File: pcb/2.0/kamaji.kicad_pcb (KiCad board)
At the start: 2 copper layers, 100 x 100 mm, 92 parts, among them J1 RJ10, J2 RJ10, J3 RJ10, J4 RJ10, J5 RJ10, J6 RJ10, J7 USB_B, J8 USB_A, Q1 2N3904, Q2 IRL540N, Q3 IRL540N, SW1 SW_Push, SW2 SW_Push, SW3 SW_Push, U1 ATMEGA32U4-AU, Y1 16MHz

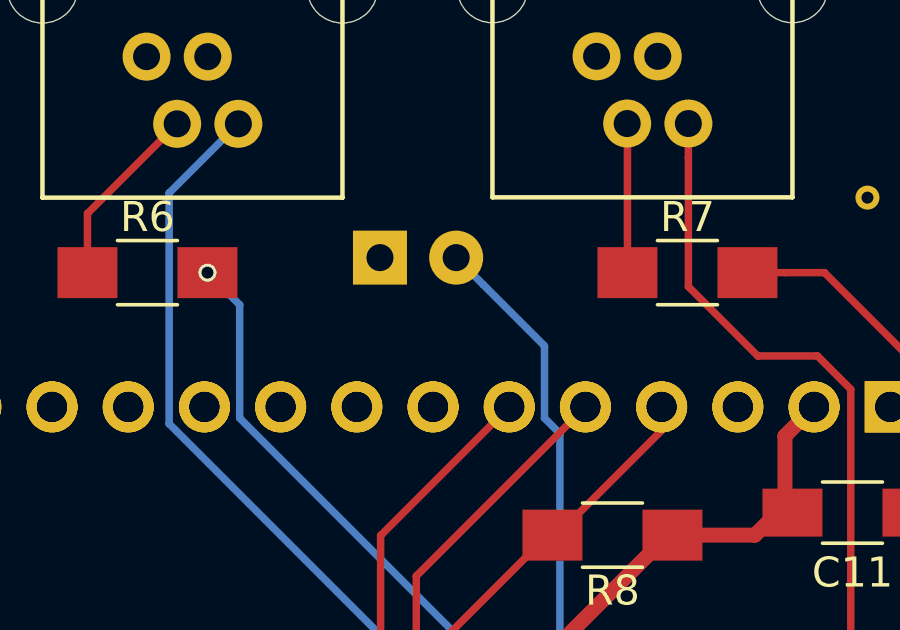
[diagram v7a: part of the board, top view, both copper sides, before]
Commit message: move the LED a bit
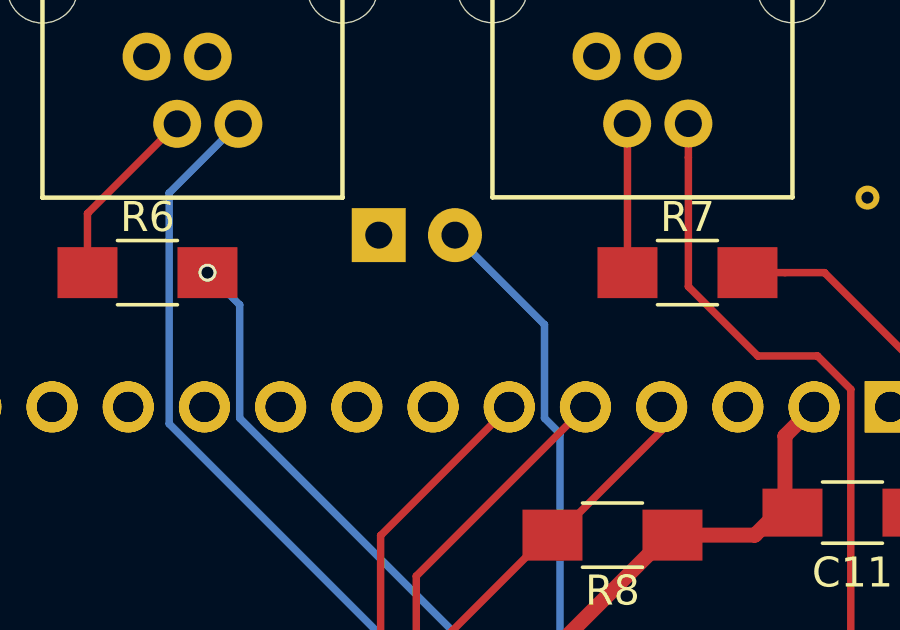
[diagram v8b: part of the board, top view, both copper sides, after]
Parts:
- moved D1 0.75 mm to (98.7, 61.2)
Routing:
- net /SIGNAL_LED: track 33.9 -> 34.7 mm
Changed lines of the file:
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@@
     (links 203)
     (no_connects 1)
-    (area 42.564999 46.54 152.093 150.075001)
+    (area 49.924999 49.924999 150.075001 150.075001)
     (thickness 1.6)
     (drawings 9)
-    (tracks 450)
+    (tracks 449)
     (zones 0)
     (modules 92)
@@
   )
   (module LEDs:LED_D5.0mm (layer B.Cu)
-    (at 98.75 62)
+    (at 98.71 61.25)
     (descr "LED, diameter 5.0mm, 2 pins, http://cdn-reichelt.de/documents/datenblatt/A500/LL-504BC2E-009.pdf")
     (tags "LED diameter 5.0mm 2 pins")
@@
   (segment (start 104 86.25) (end 104 77.25) (width 0.25) (layer B.Cu) (net 55))
   (segment (start 104 77.25) (end 104.75 76.5) (width 0.25) (layer B.Cu) (net 55))
-  (segment (start 104.233967 67.349719) (end 104.233967 64.943967) (width 0.25) (layer B.Cu) (net 55))
-  (segment (start 104.233967 64.943967) (end 102.189999 62.899999) (width 0.25) (layer B.Cu) (net 55))
   (segment (start 104.75 76.5) (end 104.75 67.865752) (width 0.25) (layer B.Cu) (net 55))
   (segment (start 104.75 67.865752) (end 104.233967 67.349719) (width 0.25) (layer B.Cu) (net 55))
-  (segment (start 102.189999 62.899999) (end 101.29 62) (width 0.25) (layer B.Cu) (net 55))
+  (segment (start 104.233967 67.349719) (end 104.233967 64.233967) (width 0.25) (layer B.Cu) (net 55))
+  (segment (start 104.233967 64.233967) (end 101.25 61.25) (width 0.25) (layer B.Cu) (net 55))
   (segment (start 99.8 92.3) (end 99.8 90.55) (width 0.25) (layer F.Cu) (net 55))
   (segment (start 99.8 90.55) (end 99.75 90.5) (width 0.25) (layer F.Cu) (net 55))
